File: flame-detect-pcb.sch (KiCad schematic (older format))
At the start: 23 parts, among them IC1 ATMEGA328-P, IC2 CH340G, P0 RELAY_(JSM1A-12V-4), Q17 Q_NPN, Q4 Q_NPN_BEC, Q5 Q_NPN_BEC, U1 NCV7805BDTRKG, X1 Crystal_GND2, X2 Crystal_GND2

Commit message: - Created circuits and footprints.
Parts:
- removed D8: D, flame-detect-pcb:R_1206_HandSoldering_(narrow), symbol D
- removed P0: RELAY_(JSM1A-12V-4), flame-detect-pcb:RELAY_(JSM1A-12V-4), symbol RELAY_(JSM1A-12V-4)
- removed Q5: Q_NPN_BEC, TO_SOT_Packages_SMD:SOT-23_Handsoldering, symbol Q_NPN_BEC
- added C3, C4: 0.01uF, flame-detect-pcb:R_1206_HandSoldering_(narrow), symbol C
- added C5, C6: 0.033uF, flame-detect-pcb:R_1206_HandSoldering_(narrow), symbol C
- added C7, C8: 10uF, Capacitors_SMD:CP_Elec_4x4.5, symbol CP
- added D1, D2: 4148, Diodes_SMD:D_SOD-323_HandSoldering, symbol D
- added Q1, Q2, Q6, Q7: MMBT2222, TO_SOT_Packages_SMD:SOT-23_Handsoldering, symbol Q_NPN_BEC
- added Q3, Q5: MMBT2907, TO_SOT_Packages_SMD:SOT-23_Handsoldering, symbol MMBT3906
- added R1, R2: 500k, flame-detect-pcb:R_1206_HandSoldering_(narrow), symbol R
- added R11, R12, R13, R14, R15, R17, R18, R6: 10k, flame-detect-pcb:R_1206_HandSoldering_(narrow), symbol R
- added R16, R3, R4: 10M, flame-detect-pcb:R_1206_HandSoldering_(narrow), symbol R
- added R5: 100k, flame-detect-pcb:R_1206_HandSoldering_(narrow), symbol R
- Q17: value Q_NPN -> MMBT2222
- Q4: value Q_NPN_BEC -> MMBT2222
- R9: value 10k -> 100k
- gave numbers to parts that had none: 1
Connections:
- net labels removed: RLY0, RLY1, RLY2, RLY3, RLY4, RLY5
- wire segments 92 -> 157
- no-connect marks 13 -> 32
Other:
- note added: "FLM_0"
- note added: "FLM_1"
- note added: "PULSE"
- note removed: "DI0"
- note removed: "DI1"
- note removed: "DI2"
- note removed: "DI3"
- note removed: "DI4"
- note removed: "DI5"
- note removed: "DO0"
- note removed: "DO1"
- note removed: "DO2"
- note removed: "DO3"
- note removed: "DO4"
- note removed: "DO5"
- moved on the sheet: C1, C2, D9, F1, IC1, IC2, Q17, Q4, R26, R27, R28, R7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

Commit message: - Finished circuit for new 8 channel version.  Ready to start on PCB.
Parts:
- removed C3, C4: 0.01uF, flame-detect-pcb:R_1206_HandSoldering_(narrow), symbol C
- removed C7, C8: 10uF, Capacitors_SMD:CP_Elec_4x4.5, symbol CP
- removed CONN_1: DEUTSCH_CONN_(DTM13-12PA-12PB-R008), flame-detect-pcb:DEUTSCH_CONN_(DTM13-12PA-12PB-R008), symbol DEUTSCH_CONN_(DTM13-12PA-12PB-R008)
- removed D2: 4148, Diodes_SMD:D_SOD-323_HandSoldering, symbol D
- removed IC1: ATMEGA328-P, Housings_DIP:DIP-28_W7.62mm_LongPads, symbol ATMEGA328-P
- removed IC2: CH340G, flame-detect-pcb:CH340G, symbol CH340G
- removed Q1, Q2, Q4, Q6, Q7: MMBT2222, TO_SOT_Packages_SMD:SOT-23_Handsoldering, symbol Q_NPN_BEC
- removed Q3, Q5: MMBT2907, TO_SOT_Packages_SMD:SOT-23_Handsoldering, symbol MMBT3906
- removed R10, R11, R12, R13, R14, R17, R18, R6, R7, R8: 10k, flame-detect-pcb:R_1206_HandSoldering_(narrow), symbol R
- removed R3, R4: 10M, flame-detect-pcb:R_1206_HandSoldering_(narrow), symbol R
- removed R5, R9: 100k, flame-detect-pcb:R_1206_HandSoldering_(narrow), symbol R
- removed U1: NCV7805BDTRKG, flame-detect-pcb:REGULATOR_(NCV7805BDTRKG), symbol NCV7805BDTRKG
- removed X1, X2: Crystal_GND2, flame-detect-pcb:RESONATOR_(CSTCE16M0V53C-R0), symbol Crystal_GND2
- added C3, C4: 47uF, Capacitors_SMD:C_0805, symbol CP
- added C7: 22pF, Capacitors_SMD:C_0805, symbol C
- added D27: LED, symbol LED
- added DIO7, DIO8, DIO9, GND_1, GND_2, V_IN_1, V_IN_2: CONN_01X01, symbol CONN_01X01
- added ICSP_1: CONN_02X03, symbol CONN_02X03
- added R67: 1K, Resistors_SMD:R_0805, symbol R
- added SERIAL_1: CONN_01X04, symbol CONN_01X04
- added U5: LM3480-5.0, TO_SOT_Packages_SMD:SOT-23, symbol LM3480-5.0
- added U6: ATMEGA328P-AU, TQFP32, symbol ATMEGA328P-AU
- added U9: DIP_SW_3, symbol DIP_SW_3
- added XTAL1: Crystal, symbol Crystal
- C1, C2: footprint flame-detect-pcb:R_1206_HandSoldering_(narrow) -> Capacitors_SMD:C_0805
- C5: value 0.033uF -> 0.1uF; footprint flame-detect-pcb:R_1206_HandSoldering_(narrow) -> Capacitors_SMD:C_0805
- C6: value 0.033uF -> 22pF; footprint flame-detect-pcb:R_1206_HandSoldering_(narrow) -> Capacitors_SMD:C_0805
- D1: value 4148 -> BAV21W-7-F; footprint Diodes_SMD:D_SOD-323_HandSoldering -> Diodes_SMD:D_0805
- F1: footprint Resistors_SMD:R_1812_HandSoldering -> Resistors_SMD:R_1812
- Q17: footprint TO_SOT_Packages_SMD:SOT-23_Handsoldering -> TO_SOT_Packages_SMD:SOT-23
- R1: value 500k -> 5.1K; footprint flame-detect-pcb:R_1206_HandSoldering_(narrow) -> Resistors_SMD:R_0805
- R15, R16, R27, R28: footprint flame-detect-pcb:R_1206_HandSoldering_(narrow) -> Resistors_SMD:R_0805
- R2: value 500k -> 560R; footprint flame-detect-pcb:R_1206_HandSoldering_(narrow) -> Resistors_SMD:R_0805
- R26: value 680 -> 680R; footprint flame-detect-pcb:R_1206_HandSoldering_(narrow) -> Resistors_SMD:R_0805
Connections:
- net GND: now also C6.1, R2.1, C3.2, C4.2, C7.1, D27.1 (K), GND_1.1 (P1), GND_2.1 (P1), ICSP_1.6 (P6), SERIAL_1.4 (P4), U5.3 (GND), U6.21 (GND), U6.3 (GND), U6.5 (GND), U9.4 (OUT_3), U9.5 (OUT_2), U9.6 (OUT_1); no longer C6.2
- net RXD: now also SERIAL_1.2 (P2), U6.30 ((PCINT16/RXD)PD0)
- net TXD: now also SERIAL_1.1 (P1), U6.31 ((PCINT17/TXD)PD1)
- net at Q17.3 (C), T1.6 (S3): now also D1.1 (K)
- net at R26.2: now also U6.10 ((PCINT22/OC0A/AIN0)PD6)
- net PULSE: now reaches R15.2
- net VBATT: now reaches R1.2
- net VBATT: now also F1.1, T1.4 (S1), C3.1, R67.2, U5.2 (VIN)
- net V_REF: now reaches R2.2
- net V_REF: now also R1.1
- net at D9.2 (A): now also V_IN_1.1 (P1), V_IN_2.1 (P1)
- net RST: now reaches C2.1, R28.2
- net RST: now also ICSP_1.5 (P5), U6.29 ((PCINT14/~RESET~)PC6)
- net at R27.1: now also C7.2, U6.8 ((PCINT7/XTAL2/TOSC2)PB7), XTAL1.1
- net at R27.2: now also C6.2, U6.7 ((PCINT6/XTAL1/TOSC1)PB6), XTAL1.2
- net at C2.2: now also SERIAL_1.3 (P3)
- net +5V renamed 5V
- net 5V: now also C5.1, C4.1, ICSP_1.2 (P2), U5.1 (VOUT), U6.18 (AVCC), U6.4 (VCC), U6.6 (VCC)
- new net: DIO7.1 (P1), U6.11 ((PCINT23/AIN1)PD7)
- new net: DIO8.1 (P1), U6.12 ((PCINT0/CLKO/ICP1)PB0)
- new net: DIO9.1 (P1), U6.13 ((PCINT1/OC1A)PB1)
- new net: D27.2 (A), R67.1
- new net ADDR_0: U6.1 ((PCINT19/OC2B/INT1)PD3), U9.1 (IN_1)
- new net ADDR_1: U6.2 ((PCINT20/XCK/T0)PD4), U9.2 (IN_2)
- new net ADDR_2: U6.9 ((PCINT21/OC0B/T1)PD5), U9.3 (IN_3)
- new net AI0: U6.23 ((PCINT8/ADC0)PC0)
- new net AI1: U6.24 ((PCINT9/ADC1)PC1)
- new net AI2: U6.25 ((PCINT10/ADC2)PC2)
- new net AI3: U6.26 ((PCINT11/ADC3)PC3)
- new net AI4: U6.27 ((PCINT12/SDA/ADC4)PC4)
- new net AI5: U6.28 ((PCINT13/SCL/ADC5)PC5)
- new net AI6: U6.19 (ADC6)
- new net AI7: U6.22 (ADC7)
- new net INT: U6.32 ((PCINT18/INT0)PD2)
- new net MISO: ICSP_1.1 (P1), U6.16 ((PCINT4/MISO)PB4)
- new net MOSI: ICSP_1.4 (P4), U6.15 ((PCINT3/OC2A/MOSI)PB3)
- new net SCK: ICSP_1.3 (P3), U6.17 ((PCINT5/SCK)PB5)
- new net SS: U6.14 ((PCINT2/OC1B/~SS~)PB2)
- no-connect marks 32 -> 3
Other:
- note removed: "D+"
- note removed: "D-"
- note removed: "FLM_0"
- note removed: "FLM_1"
- note removed: "GND"
- note removed: "IGN_IN"
- note removed: "PULSE"
- note removed: "V_BATT"
- note removed: "V_BATT_IN"
- moved on the sheet: C1, C2, D9, F1, Q17, R15, R16, R26, T1

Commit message: - Finished footprints.
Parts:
- D1: footprint Diodes_SMD:D_0805 -> Diodes_SMD:D_SOD-123
- D27: footprint (none) -> LEDs:LED_1206
- DIO7, DIO8, DIO9: footprint (none) -> flame-detect-pcb:SPARE_THROUGH_HOLE
- GND_1, GND_2, V_IN_1, V_IN_2: footprint (none) -> flame-detect-pcb:KEYSTONE_SPADE_TERM_(1287)
- ICSP_1: footprint (none) -> Pin_Headers:Pin_Header_Straight_2x03_Pitch2.54mm_SMD
- SERIAL_1: footprint (none) -> Pin_Headers:Pin_Header_Straight_1x04_Pitch2.54mm_SMD_Pin1Left
- U6: footprint TQFP32 -> Housings_QFP:TQFP-32_7x7mm_Pitch0.8mm
- U9: footprint (none) -> Buttons_Switches_SMD:SW_DIP_x3_W8.61mm_Slide_LowProfile
- XTAL1: footprint (none) -> Crystals:Crystal_SMD_HC49-SD
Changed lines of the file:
@@
 F 0 "U6" H 6000 5250 50  0000 L BNN
 F 1 "ATMEGA328P-AU" H 6950 2600 50  0000 L BNN
-F 2 "TQFP32" H 6750 4000 50  0001 C CIN
+F 2 "Housings_QFP:TQFP-32_7x7mm_Pitch0.8mm" H 6750 4000 50  0001 C CIN
 F 3 "" H 6750 4000 50  0001 C CNN
 	1    6750 4000
@@
 F 0 "V_IN_1" H 1600 1600 50  0000 C CNN
 F 1 "CONN_01X01" V 1700 1500 50  0001 C CNN
-F 2 "" H 1600 1500 50  0001 C CNN
+F 2 "flame-detect-pcb:KEYSTONE_SPADE_TERM_(1287)" H 1600 1500 50  0001 C CNN
 F 3 "" H 1600 1500 50  0001 C CNN
 	1    1600 1500
@@
 F 0 "V_IN_2" H 1600 1800 50  0000 C CNN
 F 1 "CONN_01X01" V 1700 1700 50  0001 C CNN
-F 2 "" H 1600 1700 50  0001 C CNN
+F 2 "flame-detect-pcb:KEYSTONE_SPADE_TERM_(1287)" H 1600 1700 50  0001 C CNN
 F 3 "" H 1600 1700 50  0001 C CNN
 	1    1600 1700
@@
 F 0 "GND_1" H 1600 2000 50  0000 C CNN
 F 1 "CONN_01X01" V 1700 1900 50  0001 C CNN
-F 2 "" H 1600 1900 50  0001 C CNN
+F 2 "flame-detect-pcb:KEYSTONE_SPADE_TERM_(1287)" H 1600 1900 50  0001 C CNN
 F 3 "" H 1600 1900 50  0001 C CNN
 	1    1600 1900
@@
 F 0 "GND_2" H 1600 2200 50  0000 C CNN
 F 1 "CONN_01X01" V 1700 2100 50  0001 C CNN
-F 2 "" H 1600 2100 50  0001 C CNN
+F 2 "flame-detect-pcb:KEYSTONE_SPADE_TERM_(1287)" H 1600 2100 50  0001 C CNN
 F 3 "" H 1600 2100 50  0001 C CNN
 	1    1600 2100
@@
 F 0 "ICSP_1" H 1950 3250 50  0000 C CNN
 F 1 "CONN_02X03" H 1950 2850 50  0001 C CNN
-F 2 "" H 1950 1850 50  0001 C CNN
+F 2 "Pin_Headers:Pin_Header_Straight_2x03_Pitch2.54mm_SMD" H 1950 1850 50  0001 C CNN
 F 3 "" H 1950 1850 50  0001 C CNN
 	1    1950 3050
@@
 F 0 "SERIAL_1" H 1950 4150 50  0000 C CNN
 F 1 "CONN_01X04" V 2050 3900 50  0001 C CNN
-F 2 "" H 1950 3900 50  0001 C CNN
+F 2 "Pin_Headers:Pin_Header_Straight_1x04_Pitch2.54mm_SMD_Pin1Left" H 1950 3900 50  0001 C CNN
 F 3 "" H 1950 3900 50  0001 C CNN
 	1    1950 3900
@@
 F 0 "XTAL1" H 8600 3850 50  0000 C CNN
 F 1 "Crystal" H 8600 3550 50  0001 C CNN
-F 2 "" H 8600 3700 50  0001 C CNN
+F 2 "Crystals:Crystal_SMD_HC49-SD" H 8600 3700 50  0001 C CNN
 F 3 "" H 8600 3700 50  0001 C CNN
 	1    8600 3700
@@
 F 0 "D1" H 10550 5350 50  0000 C CNN
 F 1 "BAV21W-7-F" H 10550 5150 50  0000 C CNN
-F 2 "Diodes_SMD:D_0805" H 10550 5250 50  0001 C CNN
+F 2 "Diodes_SMD:D_SOD-123" H 10550 5250 50  0001 C CNN
 F 3 "" H 10550 5250 50  0001 C CNN
 	1    10550 5250
@@
 F 0 "DIO8" H 8250 2900 50  0000 C CNN
 F 1 "CONN_01X01" V 8200 2900 50  0001 C CNN
-F 2 "" H 8100 2900 50  0001 C CNN
+F 2 "flame-detect-pcb:SPARE_THROUGH_HOLE" H 8100 2900 50  0001 C CNN
 F 3 "" H 8100 2900 50  0001 C CNN
 	1    8100 2900
@@
 F 0 "DIO9" H 8600 3000 50  0000 C CNN
 F 1 "CONN_01X01" V 8550 3000 50  0001 C CNN
-F 2 "" H 8450 3000 50  0001 C CNN
+F 2 "flame-detect-pcb:SPARE_THROUGH_HOLE" H 8450 3000 50  0001 C CNN
 F 3 "" H 8450 3000 50  0001 C CNN
 	1    8450 3000
@@
 F 0 "DIO7" H 8250 5200 50  0000 C CNN
 F 1 "CONN_01X01" V 8200 5200 50  0001 C CNN
-F 2 "" H 8100 5200 50  0001 C CNN
+F 2 "flame-detect-pcb:SPARE_THROUGH_HOLE" H 8100 5200 50  0001 C CNN
 F 3 "" H 8100 5200 50  0001 C CNN
 	1    8100 5200
@@
 F 0 "U9" H 1900 4700 50  0000 L CNN
 F 1 "DIP_SW_3" H 1900 5200 50  0000 L CNN
-F 2 "" H 1900 4600 50  0001 L CNN
+F 2 "Buttons_Switches_SMD:SW_DIP_x3_W8.61mm_Slide_LowProfile" H 1900 4600 50  0001 L CNN
 F 3 "" H 2300 4600 60  0001 C CNN
 	1    2150 4950
@@
 F 0 "D27" H 3400 2350 50  0000 C CNN
 F 1 "LED" H 3400 2150 50  0000 C CNN
-F 2 "" H 3400 2250 50  0001 C CNN
+F 2 "LEDs:LED_1206" H 3400 2250 50  0001 C CNN
 F 3 "" H 3400 2250 50  0001 C CNN
 	1    3400 2250

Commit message: - Finished PCB layout.
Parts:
- added GND_3, GND_4, GND_5, GND_6: CONN_01X01, flame-detect-pcb:PEM_STANDOFF_THRU_(SMTSOB-116-12ET), symbol CONN_01X01
- C3, C4: footprint Capacitors_SMD:C_0805 -> Capacitors_SMD:CP_Elec_6.3x5.3
- renumbered U9 to CAN_ADDR_1
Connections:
- net 5V: no longer ICSP_1.2 (P2)
- net GND: now also T1.7 (GND), T1.8 (GND), GND_3.1 (P1), GND_4.1 (P1), GND_5.1 (P1), GND_6.1 (P1)
- no-connect marks 3 -> 4
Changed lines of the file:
@@
 F 0 "C3" H 3875 1900 50  0000 L CNN
 F 1 "47uF" H 3875 1700 50  0000 L CNN
-F 2 "Capacitors_SMD:C_0805" H 3888 1650 50  0001 C CNN
+F 2 "Capacitors_SMD:CP_Elec_6.3x5.3" H 3888 1650 50  0001 C CNN
 F 3 "" H 3850 1800 50  0001 C CNN
 	1    3850 1800
@@
 F 0 "C4" H 4975 1900 50  0000 L CNN
 F 1 "47uF" H 4975 1700 50  0000 L CNN
-F 2 "Capacitors_SMD:C_0805" H 4988 1650 50  0001 C CNN
+F 2 "Capacitors_SMD:CP_Elec_6.3x5.3" H 4988 1650 50  0001 C CNN
 F 3 "" H 4950 1800 50  0001 C CNN
 	1    4950 1800
@@
 Connection ~ 5750 1500
 Text GLabel 8550 4350 2    60   Input ~ 0
-5V
-Text GLabel 2200 2950 2    60   Input ~ 0
 5V
 Text GLabel 2200 3050 2    60   Input ~ 0
@@
 L GND #PWR010
 U 1 1 5AAFDA89
-P 9300 2800
-F 0 "#PWR010" H 9300 2550 50  0001 C CNN
-F 1 "GND" H 9300 2650 50  0000 C CNN
-F 2 "" H 9300 2800 50  0000 C CNN
-F 3 "" H 9300 2800 50  0000 C CNN
-	1    9300 2800
-	1    0    0    -1
-$EndComp
-Wire Wire Line
-	9300 2500 9300 2800
+P 9300 2950
+F 0 "#PWR010" H 9300 2700 50  0001 C CNN
+F 1 "GND" H 9300 2800 50  0000 C CNN
+F 2 "" H 9300 2950 50  0000 C CNN
+F 3 "" H 9300 2950 50  0000 C CNN
+	1    9300 2950
+	1    0    0    -1
+$EndComp
+Wire Wire Line
+	9300 2500 9300 2950
 $Sheet
 S 1600 7050 750  300
@@
 $EndSheet
 $Comp
-L DIP_SW_3 U9
+L DIP_SW_3 CAN_ADDR_1
 U 1 1 5AB0433E
 P 2150 4950
-F 0 "U9" H 1900 4700 50  0000 L CNN
+F 0 "CAN_ADDR_1" H 1900 4700 50  0000 L CNN
 F 1 "DIP_SW_3" H 1900 5200 50  0000 L CNN
 F 2 "Buttons_Switches_SMD:SW_DIP_x3_W8.61mm_Slide_LowProfile" H 1900 4600 50  0001 L CNN
@@
 Wire Wire Line
 	3400 2400 3400 2500
+NoConn ~ 2200 2950
+$Comp
+L CONN_01X01 GND_3
+U 1 1 5AB1BFEB
+P 4100 3200
+F 0 "GND_3" H 4100 3300 50  0000 C CNN
+F 1 "CONN_01X01" V 4200 3200 50  0001 C CNN
+F 2 "flame-detect-pcb:PEM_STANDOFF_THRU_(SMTSOB-116-12ET)" H 4100 3200 50  0001 C CNN
+F 3 "" H 4100 3200 50  0001 C CNN
+	1    4100 3200
+	-1   0    0    1
+$EndComp
+$Comp
+L CONN_01X01 GND_4
+U 1 1 5AB1C0FB
+P 4100 3400
+F 0 "GND_4" H 4100 3500 50  0000 C CNN
+F 1 "CONN_01X01" V 4200 3400 50  0001 C CNN
+F 2 "flame-detect-pcb:PEM_STANDOFF_THRU_(SMTSOB-116-12ET)" H 4100 3400 50  0001 C CNN
+F 3 "" H 4100 3400 50  0001 C CNN
+	1    4100 3400
+	-1   0    0    1
+$EndComp
+$Comp
+L CONN_01X01 GND_5
+U 1 1 5AB1C18B
+P 4100 3600
+F 0 "GND_5" H 4100 3700 50  0000 C CNN
+F 1 "CONN_01X01" V 4200 3600 50  0001 C CNN
+F 2 "flame-detect-pcb:PEM_STANDOFF_THRU_(SMTSOB-116-12ET)" H 4100 3600 50  0001 C CNN
+F 3 "" H 4100 3600 50  0001 C CNN
+	1    4100 3600
+	-1   0    0    1
+$EndComp
+$Comp
+L CONN_01X01 GND_6
+U 1 1 5AB1C20E
+P 4100 3800
+F 0 "GND_6" H 4100 3900 50  0000 C CNN
+F 1 "CONN_01X01" V 4200 3800 50  0001 C CNN
+F 2 "flame-detect-pcb:PEM_STANDOFF_THRU_(SMTSOB-116-12ET)" H 4100 3800 50  0001 C CNN
+F 3 "" H 4100 3800 50  0001 C CNN
+	1    4100 3800
+	-1   0    0    1
+$EndComp
+$Comp
+L GND #PWR013
+U 1 1 5AB1C400
+P 4450 3950
+F 0 "#PWR013" H 4450 3700 50  0001 C CNN
+F 1 "GND" H 4450 3800 50  0000 C CNN
+F 2 "" H 4450 3950 50  0000 C CNN
+F 3 "" H 4450 3950 50  0000 C CNN
+	1    4450 3950
+	1    0    0    -1
+$EndComp
+Wire Wire Line
+	4300 3200 4450 3200
+Wire Wire Line
+	4450 3200 4450 3950
+Wire Wire Line
+	4300 3400 4450 3400
+Connection ~ 4450 3400
+Wire Wire Line
+	4300 3600 4450 3600
+Connection ~ 4450 3600
+Wire Wire Line
+	4300 3800 4450 3800
+Connection ~ 4450 3800
+Wire Wire Line
+	9550 2750 9300 2750
+Connection ~ 9300 2750
+Wire Wire Line
+	10350 2750 10350 2850
+Wire Wire Line
+	10350 2850 9300 2850
+Connection ~ 9300 2850
 $EndSCHEMATC

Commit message: - Fixed several bugs.
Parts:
- added C28: 0.1uF, Capacitors_SMD:C_0805, symbol C
- D9: footprint flame-detect-pcb:SCHOTTKY_(PMEG3030EP,115) -> flame-detect-pcb:DO-214AB
- SERIAL_1: footprint Pin_Headers:Pin_Header_Straight_1x04_Pitch2.54mm_SMD_Pin1Left -> Pin_Headers:Pin_Header_Straight_1x04_Pitch2.54mm_SMD_Pin1Right
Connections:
- net 5V: now also ICSP_1.2 (P2)
- net GND: now also C28.2
- net at U6.20 (AREF): now also C28.1
- no-connect marks 4 -> 2
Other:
- moved on the sheet: C1
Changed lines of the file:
@@
 F 0 "D9" H 2450 1600 50  0000 C CNN
 F 1 "D_Schottky" H 2450 1400 50  0000 C CNN
-F 2 "flame-detect-pcb:SCHOTTKY_(PMEG3030EP,115)" H 2450 1500 50  0001 C CNN
+F 2 "flame-detect-pcb:DO-214AB" H 2450 1500 50  0001 C CNN
 F 3 "" H 2450 1500 50  0000 C CNN
 	1    2450 1500
@@
 L C C1
 U 1 1 58106D06
-P 5750 3850
-F 0 "C1" H 5775 3950 50  0000 L CNN
-F 1 "0.1uF" H 5775 3750 50  0000 L CNN
-F 2 "Capacitors_SMD:C_0805" H 5788 3700 50  0001 C CNN
-F 3 "" H 5750 3850 50  0000 C CNN
-	1    5750 3850
+P 5750 3750
+F 0 "C1" H 5775 3850 50  0000 L CNN
+F 1 "0.1uF" H 5775 3650 50  0000 L CNN
+F 2 "Capacitors_SMD:C_0805" H 5788 3600 50  0001 C CNN
+F 3 "" H 5750 3750 50  0000 C CNN
+	1    5750 3750
 	1    0    0    -1
 $EndComp
@@
 	0    1    1    0
 $EndComp
-NoConn ~ 5850 3500
 $Comp
 L TRANSFORMER_(42TL013-RC) T1
@@
 Connection ~ 5750 5200
 Wire Wire Line
-	5750 4000 5750 5300
+	5750 3900 5750 5300
 Wire Wire Line
 	7750 3500 8700 3500
@@
 RST
 Wire Wire Line
-	5750 1500 5750 3700
+	5750 1500 5750 3600
 Text GLabel 5900 1500 2    60   Input ~ 0
 5V
@@
 F 0 "SERIAL_1" H 1950 4150 50  0000 C CNN
 F 1 "CONN_01X04" V 2050 3900 50  0001 C CNN
-F 2 "Pin_Headers:Pin_Header_Straight_1x04_Pitch2.54mm_SMD_Pin1Left" H 1950 3900 50  0001 C CNN
+F 2 "Pin_Headers:Pin_Header_Straight_1x04_Pitch2.54mm_SMD_Pin1Right" H 1950 3900 50  0001 C CNN
 F 3 "" H 1950 3900 50  0001 C CNN
 	1    1950 3900
@@
 Wire Wire Line
 	3400 2400 3400 2500
-NoConn ~ 2200 2950
 $Comp
 L CONN_01X01 GND_3
@@
 	10350 2850 9300 2850
 Connection ~ 9300 2850
+Text GLabel 2200 2950 2    60   Input ~ 0
+5V
+$Comp
+L C C28
+U 1 1 5ABBE8B1
+P 5150 3750
+F 0 "C28" H 5175 3850 50  0000 L CNN
+F 1 "0.1uF" H 5175 3650 50  0000 L CNN
+F 2 "Capacitors_SMD:C_0805" H 5188 3600 50  0001 C CNN
+F 3 "" H 5150 3750 50  0000 C CNN
+	1    5150 3750
+	1    0    0    -1
+$EndComp
+Wire Wire Line
+	5850 3500 5150 3500
+Wire Wire Line
+	5150 3500 5150 3600
+$Comp
+L GND #PWR014
+U 1 1 5ABBEA1E
+P 5150 3950
+F 0 "#PWR014" H 5150 3700 50  0001 C CNN
+F 1 "GND" H 5150 3800 50  0000 C CNN
+F 2 "" H 5150 3950 50  0000 C CNN
+F 3 "" H 5150 3950 50  0000 C CNN
+	1    5150 3950
+	1    0    0    -1
+$EndComp
+Wire Wire Line
+	5150 3900 5150 3950
 $EndSCHEMATC

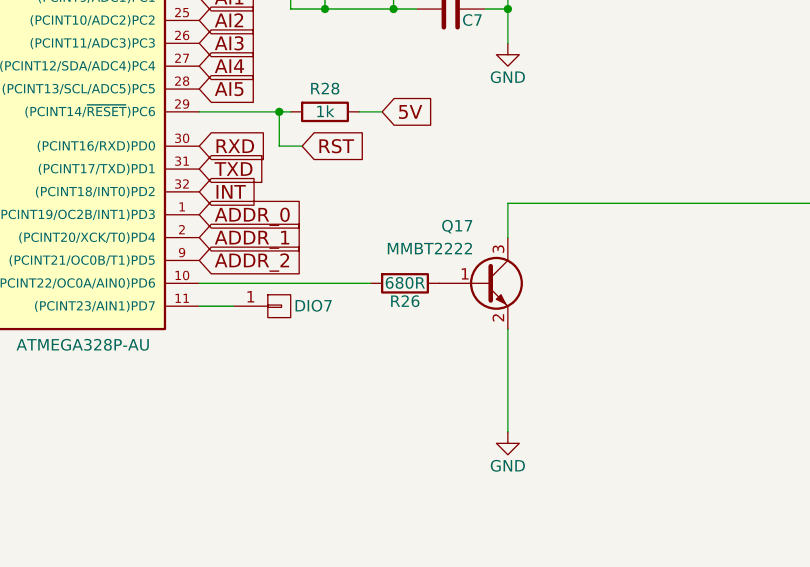
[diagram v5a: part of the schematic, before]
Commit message: - Changed transformer transistor resistor to 10kohm.
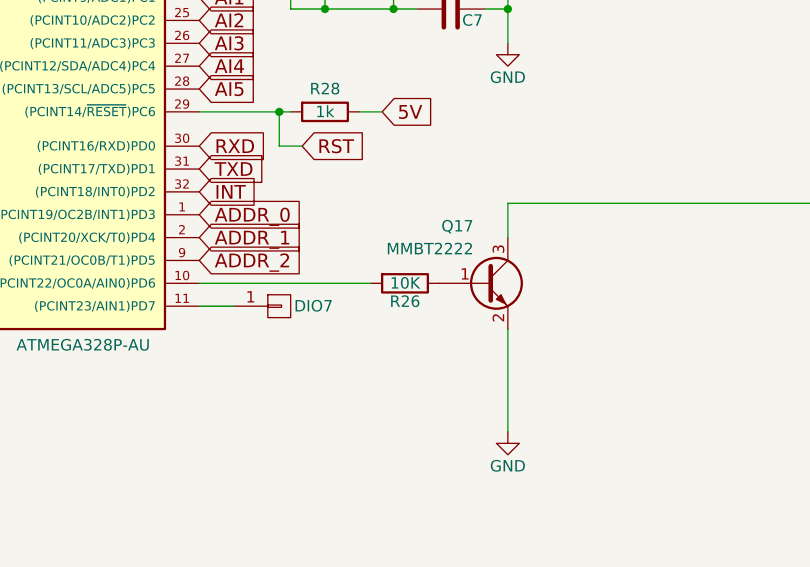
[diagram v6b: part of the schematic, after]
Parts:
- R26: value 680R -> 10K
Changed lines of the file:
@@
 P 8650 5100
 F 0 "R26" V 8730 5100 50  0000 C CNN
-F 1 "680R" V 8650 5100 50  0000 C CNN
+F 1 "10K" V 8650 5100 50  0000 C CNN
 F 2 "Resistors_SMD:R_0805" V 8580 5100 50  0001 C CNN
 F 3 "" H 8650 5100 50  0000 C CNN
